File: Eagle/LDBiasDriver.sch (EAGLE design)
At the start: 23 parts, among them IC1 MCP1703-5002E/DB, IC2 MLD203P1, IC3 LM358D

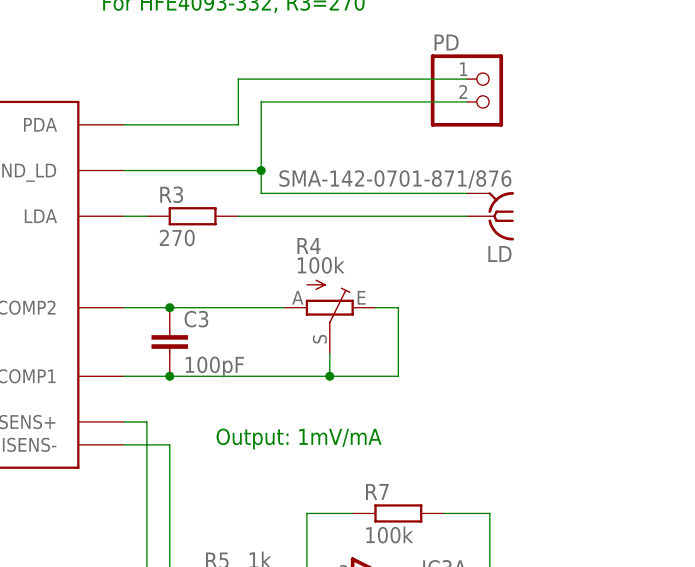
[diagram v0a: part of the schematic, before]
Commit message: used a standard connector spacing for the SMA alternative.
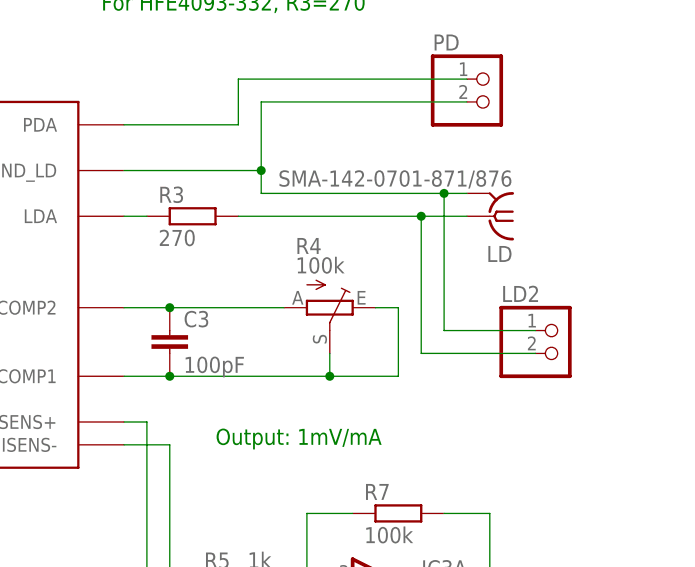
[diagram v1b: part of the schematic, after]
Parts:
- added LD2: (no value), pinhead:PINHD-1X2
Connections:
- net N$10: now also LD2.1
- net N$8: now also LD2.2
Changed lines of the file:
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@@
 <part name="LED1" library="led" deviceset="LED" device="CHIPLED_1206"/>
 <part name="R2" library="rcl" deviceset="R-EU_" device="R0805" value="1k"/>
+<part name="LD2" library="pinhead" deviceset="PINHD-1X2" device=""/>
 </parts>
 <sheets>
@@
 <instance part="LED1" gate="G$1" x="-30.48" y="22.86"/>
 <instance part="R2" gate="G$1" x="-30.48" y="30.48" rot="R90"/>
+<instance part="LD2" gate="G$1" x="104.14" y="38.1"/>
 </instances>
 <busses>
@@
 <pinref part="R3" gate="G$1" pin="2"/>
 <pinref part="LD" gate="G1" pin="1"/>
-<wire x1="68.58" y1="53.34" x2="93.98" y2="53.34" width="0.1524" layer="91"/>
+<wire x1="68.58" y1="53.34" x2="88.9" y2="53.34" width="0.1524" layer="91"/>
+<pinref part="LD2" gate="G$1" pin="2"/>
+<wire x1="88.9" y1="53.34" x2="93.98" y2="53.34" width="0.1524" layer="91"/>
+<wire x1="101.6" y1="38.1" x2="88.9" y2="38.1" width="0.1524" layer="91"/>
+<wire x1="88.9" y1="38.1" x2="88.9" y2="53.34" width="0.1524" layer="91"/>
+<junction x="88.9" y="53.34"/>
 </segment>
 </net>
@@
 <segment>
 <pinref part="LD" gate="G1" pin="2"/>
-<wire x1="93.98" y1="55.88" x2="71.12" y2="55.88" width="0.1524" layer="91"/>
+<wire x1="93.98" y1="55.88" x2="91.44" y2="55.88" width="0.1524" layer="91"/>
+<wire x1="91.44" y1="55.88" x2="71.12" y2="55.88" width="0.1524" layer="91"/>
 <wire x1="71.12" y1="55.88" x2="71.12" y2="58.42" width="0.1524" layer="91"/>
 <pinref part="IC2" gate="G$1" pin="GND_LD"/>
@@
 <wire x1="71.12" y1="66.04" x2="71.12" y2="58.42" width="0.1524" layer="91"/>
 <junction x="71.12" y="58.42"/>
+<pinref part="LD2" gate="G$1" pin="1"/>
+<wire x1="101.6" y1="40.64" x2="91.44" y2="40.64" width="0.1524" layer="91"/>
+<wire x1="91.44" y1="40.64" x2="91.44" y2="55.88" width="0.1524" layer="91"/>
+<junction x="91.44" y="55.88"/>
 </segment>
 </net>

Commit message: Updates based on experience
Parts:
- LD: value SMA-142-0701-871/876 -> SMA-142-0711-821/826; device con-coax:SMA-142-0701-871/876 -> con-coax:SMA-142-0711-821/826
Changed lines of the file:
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@@
 <part name="C2" library="rcl" deviceset="C-EU" device="C0805" value="10uF"/>
 <part name="R1" library="pot" deviceset="TRIM_EU-" device="RJ9W" value="10k"/>
-<part name="LD" library="con-coax" deviceset="SMA-" device="142-0701-871/876"/>
+<part name="LD" library="con-coax" deviceset="SMA-" device="142-0711-821/826" value="SMA-142-0711-821/826"/>
 <part name="R3" library="rcl" deviceset="R-EU_" device="R0805" value="270"/>
 <part name="IC2" library="laser diode" deviceset="MLD203P1" device=""/>
